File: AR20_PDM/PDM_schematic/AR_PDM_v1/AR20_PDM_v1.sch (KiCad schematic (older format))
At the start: 23 parts, among them J1 S_T_?, J2 1-776163-1, U1 ACM_2020

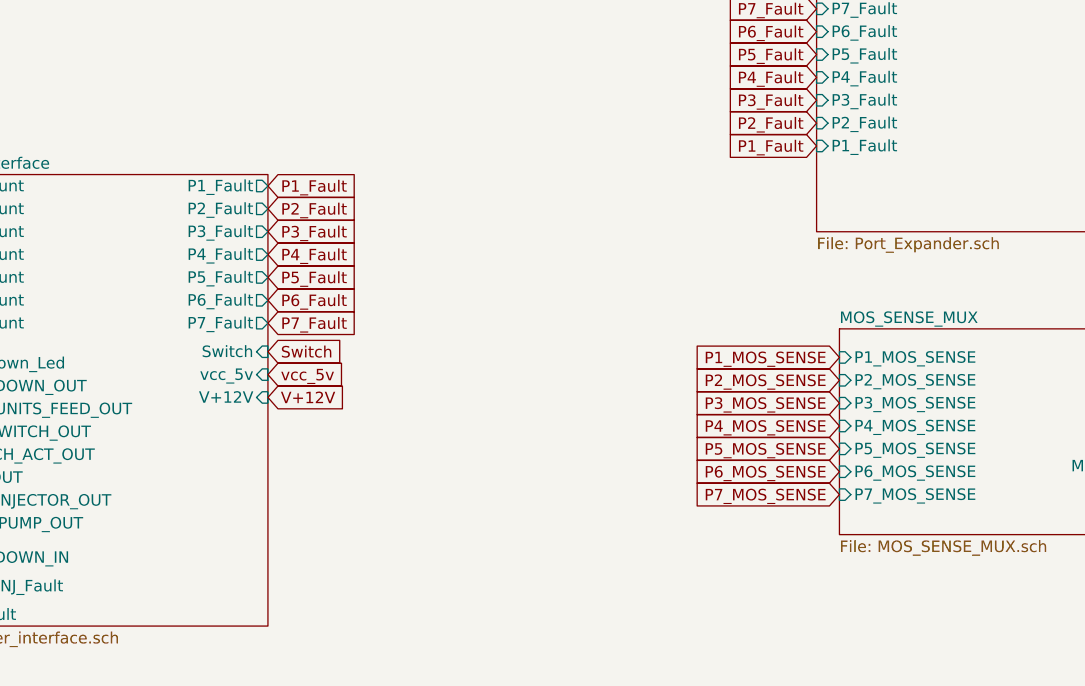
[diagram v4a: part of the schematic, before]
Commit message: Further testing, reveals pdm needs rework
-  As of now, there are major errors in schematics.
- Needs rework. Version charlie postponed.
- Very nice pcb layout thats almost finished. 
   worth noting this layout for the future
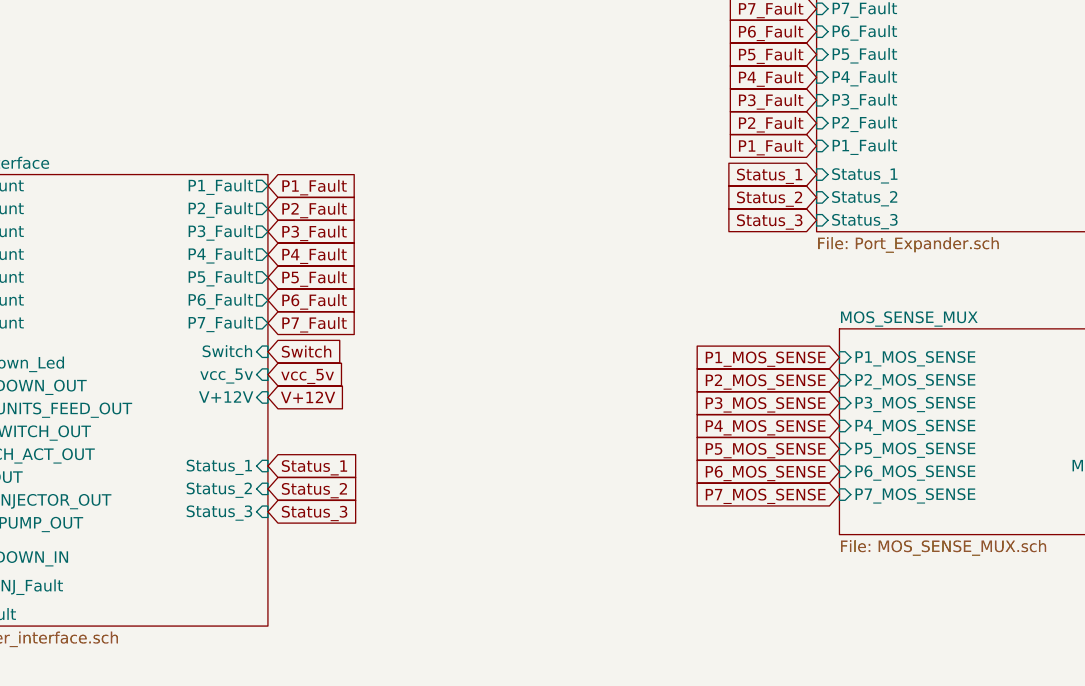
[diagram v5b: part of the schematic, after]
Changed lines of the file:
@@
 F28 "P7_Shunt" I L 4375 4650 50
 F29 "P1_Shunt" I L 4375 4050 50
+F30 "Status_2" I R 5825 5375 50
+F31 "Status_1" I R 5825 5275 50
+F32 "Status_3" I R 5825 5475 50
 $EndSheet
 Text GLabel 10050 3200 2    50   Input ~ 0
@@
 F17 "Mux_select_A2" I R 10050 3400 50
 F18 "Mux_enable" I R 10050 3500 50
+F19 "Status_2" I L 8225 4100 50
+F20 "Status_1" I L 8225 4000 50
+F21 "Status_3" I L 8225 4200 50
 $EndSheet
 NoConn ~ 7900 1275
@@
 Text GLabel 11850 2850 1    50   Input ~ 0
 vcc_5v
+Text GLabel 5825 5275 2    50   Input ~ 0
+Status_1
+Text GLabel 5825 5375 2    50   Input ~ 0
+Status_2
+Text GLabel 5825 5475 2    50   Input ~ 0
+Status_3
+Text GLabel 8225 4000 0    50   Input ~ 0
+Status_1
+Text GLabel 8225 4100 0    50   Input ~ 0
+Status_2
+Text GLabel 8225 4200 0    50   Input ~ 0
+Status_3
 $EndSCHEMATC

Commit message: schematics rework
Fixed INA233 frying due to inductive flyback:
- Paced ina233 high side of the mosftets
- New input protection reseistors, and zener diodes, on each ina233.
Simplified:
- Removed the MUX and mos sense lines, as i realize that most of this functionality can be obtained trough INA233.
- Removed some of the cappacitors , besides the most needed ones.
- removed  back to back zener diode configuration, now a single diode insted.
 to reduce negative voltage in case of loss of VS, to be easy on the INA233 filters.
new stuff:
- Another temp sensor.
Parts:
- removed C4, C5: 470uf, AR_PDM_v1:CAPAE1350X1400N_EEV-FK1V471Q, symbol AR20_PDM_v1-rescue:CP1
- removed C6: 10nf, Capacitor_SMD:C_0603_1608Metric, symbol AR20_PDM_v1-rescue:C-Device
- removed D2, D4: 3.3-5V 5W, Diode_THT:D_5W_P10.16mm_Horizontal, symbol AR20_PDM_v1-rescue:D_Flyback-Zener
- removed R1: 1k, Resistor_SMD:R_0603_1608Metric, symbol AR20_PDM_v1-rescue:R-Device
- removed R2: 4k7, Resistor_SMD:R_0603_1608Metric, symbol AR20_PDM_v1-rescue:R-Device
- added C?: 4.7uF, Capacitor_SMD:C_1206_3216Metric, symbol AR20_PDM_v1-rescue:C-Device
- added R?: 3.9R, Resistor_SMD:R_2512_6332Metric, symbol AR20_PDM_v1-rescue:R-Device
- added R?: NTC, Resistor_SMD:R_0603_1608Metric, symbol AR20_PDM_v1-rescue:R-Device
- added R?: 1k, Resistor_SMD:R_0603_1608Metric, symbol AR20_PDM_v1-rescue:R-Device
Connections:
- net GND: now also D1.2 (A), D3.2 (A), U1.19 (GND), U1.9 (GND), C?.1, R?.1
- net V+12V: now also R?.1
- net vcc_5v: now also R?.1
- net at U1.5 (ADC7): now also R?.2, R?.2
- new net: C?.2, R?.2
- no-connect marks 12 -> 10
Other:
- note added: "Snubber to prevent,\nOscillations on VS line.\nApplication note; \nintroduction to PROFET, page 12"
- note added: "eLoss of power, flyback protection. \nPlace relativly near all of the mosfets.\nApplication note; \nintroduction to PROFET, page 12\nTo keep negative voltage spike low, a single diode in series is used.\nTwo for redundancy\n"
- note removed: "Loss of power, flyback protection. \nPlace relativly near all of the mosfets."
- note removed: "Place relativly close to mcu"
- note removed: "Shared sensing circuit for mosfets."
- moved on the sheet: C1, C2, C3, D1, D3, J1, R106, R107

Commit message: Working on pcb layout
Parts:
- gave numbers to parts that had none: 4
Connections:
- no-connect marks 10 -> 17
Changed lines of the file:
@@
 Text GLabel 7900 950  0    50   Input ~ 0
 vcc_5v
-Wire Wire Line
-	2225 875  2125 875
 $Sheet
 S 1100 625  1025 525
@@
 F7 "P1_MOS_SENSE" O R 2125 875 50
 F8 "P1_MOS_IN" O L 1100 1100 50
-F9 "P1_Shunt" I R 2125 1075 50
 $EndSheet
-Text GLabel 2225 875  2    50   Input ~ 0
-P1_MOS_SENSE
 Wire Wire Line
 	1000 1100 1100 1100
@@
 vcc_5v
 Wire Wire Line
-	2225 1650 2125 1650
-Text GLabel 2225 1650 2    50   Input ~ 0
-P2_MOS_SENSE
-Wire Wire Line
 	1000 1875 1100 1875
 Text GLabel 1000 1875 0    50   Input ~ 0
@@
 Text GLabel 1000 1450 0    50   Input ~ 0
 vcc_5v
-Wire Wire Line
-	2225 2400 2125 2400
 $Sheet
 S 1100 2150 1025 525
@@
 F7 "P3_OUT" O R 2125 2500 50
 F8 "P3_MOS_IN" O L 1100 2625 50
-F9 "P3_Shunt" I R 2125 2600 50
 $EndSheet
-Text GLabel 2225 2400 2    50   Input ~ 0
-P3_MOS_SENSE
 Wire Wire Line
 	1000 2625 1100 2625
@@
 vcc_5v
 Wire Wire Line
-	2225 3150 2125 3150
-Text GLabel 2225 3150 2    50   Input ~ 0
-P4_MOS_SENSE
-Wire Wire Line
 	1000 3375 1100 3375
 Text GLabel 1000 3375 0    50   Input ~ 0
@@
 Text GLabel 1000 2950 0    50   Input ~ 0
 vcc_5v
-Wire Wire Line
-	2225 3900 2125 3900
 $Sheet
 S 1100 3650 1025 525
@@
 F7 "P5_OUT" O R 2125 4000 50
 F8 "P5_MOS_IN" O L 1100 4125 50
-F9 "P5_Shunt" I R 2125 4100 50
 $EndSheet
-Text GLabel 2225 3900 2    50   Input ~ 0
-P5_MOS_SENSE
 Wire Wire Line
 	1000 4125 1100 4125
@@
 Text GLabel 1000 3700 0    50   Input ~ 0
 vcc_5v
-Wire Wire Line
-	2225 4650 2125 4650
 $Sheet
 S 1100 4400 1025 525
@@
 F8 "P6_MOS_IN" O L 1100 4875 50
 F9 "P6_O_D_out" I R 2125 4475 50
-F10 "P6_Shunt" I R 2125 4850 50
 $EndSheet
-Text GLabel 2225 4650 2    50   Input ~ 0
-P6_MOS_SENSE
 Wire Wire Line
 	1000 4875 1100 4875
@@
 Wire Wire Line
 	1125 9100 1125 8850
-Wire Wire Line
-	2225 5400 2125 5400
-Text GLabel 2225 5400 2    50   Input ~ 0
-P7_MOS_SENSE
 Wire Wire Line
 	1000 5625 1100 5625
@@
 F7 "P2_OUT" O R 2125 1750 50
 F8 "P2_MOS_IN" O L 1100 1875 50
-F9 "P2_Shunt" I R 2125 1850 50
 $EndSheet
 $Sheet
@@
 F7 "P4_OUT" O R 2125 3250 50
 F8 "P4_MOS_IN" O L 1100 3375 50
-F9 "P4_Shunt" I R 2125 3350 50
 $EndSheet
 $Sheet
@@
 F7 "P7_OUT" O R 2125 5500 50
 F8 "P7_MOS_IN" O L 1100 5625 50
-F9 "P7_Shunt" I R 2125 5600 50
 $EndSheet
 Wire Wire Line
@@
 Wire Wire Line
 	2225 4750 2125 4750
-Text GLabel 2225 4000 2    50   Input ~ 0
-P5_OUT
-Wire Wire Line
-	2225 4000 2125 4000
 Text GLabel 2225 3250 2    50   Input ~ 0
 P4_OUT
@@
 Text GLabel 8000 750  0    50   Input ~ 0
 SHUTDOWN_IN
-Text GLabel 4375 4650 0    50   Input ~ 0
-P7_Shunt
-Text GLabel 4375 4550 0    50   Input ~ 0
-P6_Shunt
-Text GLabel 4375 4450 0    50   Input ~ 0
-P5_Shunt
-Text GLabel 4375 4350 0    50   Input ~ 0
-P4_Shunt
-Text GLabel 4375 4250 0    50   Input ~ 0
-P3_Shunt
-Text GLabel 4375 4150 0    50   Input ~ 0
-P2_Shunt
-Text GLabel 4375 4050 0    50   Input ~ 0
-P1_Shunt
 Text GLabel 4375 5425 0    50   Input ~ 0
 COIL_INJECTOR_OUT
@@
 Wire Wire Line
 	11425 8475 11425 8675
-Text GLabel 2225 5600 2    50   Input ~ 0
-P7_Shunt
-Text GLabel 2225 4850 2    50   Input ~ 0
-P6_Shunt
-Text GLabel 2225 4100 2    50   Input ~ 0
-P5_Shunt
-Text GLabel 2225 3350 2    50   Input ~ 0
-P4_Shunt
-Text GLabel 2225 2600 2    50   Input ~ 0
-P3_Shunt
-Text GLabel 2225 1850 2    50   Input ~ 0
-P2_Shunt
-Text GLabel 2225 1075 2    50   Input ~ 0
-P1_Shunt
-Wire Wire Line
-	2225 5600 2125 5600
-Wire Wire Line
-	2225 4850 2125 4850
-Wire Wire Line
-	2225 4100 2125 4100
-Wire Wire Line
-	2225 3350 2125 3350
-Wire Wire Line
-	2225 2600 2125 2600
-Wire Wire Line
-	2225 1850 2125 1850
-Wire Wire Line
-	2225 1075 2125 1075
 Text GLabel 13625 975  0    50   Input ~ 0
 P6_EN_ACM
@@
 F21 "Shutdown_Led" I L 4375 4825 50
 F22 "SHUTDOWN_IN" I L 4375 5675 50
-F23 "P2_Shunt" I L 4375 4150 50
-F24 "P3_Shunt" I L 4375 4250 50
-F25 "P4_Shunt" I L 4375 4350 50
-F26 "P5_Shunt" I L 4375 4450 50
-F27 "P6_Shunt" I L 4375 4550 50
-F28 "P7_Shunt" I L 4375 4650 50
-F29 "P1_Shunt" I L 4375 4050 50
-F30 "Status_2" I R 5825 5375 50
-F31 "Status_1" I R 5825 5275 50
-F32 "Status_3" I R 5825 5475 50
+F23 "Status_2" I R 5825 5375 50
+F24 "Status_1" I R 5825 5275 50
+F25 "Status_3" I R 5825 5475 50
+F26 "P2_OUT" I L 4375 4175 50
+F27 "P3_OUT" I L 4375 4275 50
+F28 "P4_OUT" I L 4375 4375 50
+F29 "P5_OUT" I L 4375 4475 50
+F30 "P6_OUT" I L 4375 4575 50
+F31 "P7_OUT" I L 4375 4675 50
+F32 "P1_OUT" I L 4375 4075 50
 $EndSheet
 Text GLabel 15175 2475 2    50   Input ~ 0
@@
 AR Path="/5E0FDCCC/5EE38514" Ref="C?"  Part="1"
 AR Path="/5E10174B/5EE38514" Ref="C?"  Part="1"
-AR Path="/5EE38514" Ref="C?"  Part="1"
-F 0 "C?" H 6165 9246 50  0000 L CNN
+AR Path="/5EE38514" Ref="C4"  Part="1"
+F 0 "C4" H 6165 9246 50  0000 L CNN
 F 1 "4.7uF" H 6165 9155 50  0000 L CNN
 F 2 "Capacitor_SMD:C_1206_3216Metric" H 6088 9050 50  0001 C CNN
@@
 AR Path="/5E0FDCCC/5EE3851A" Ref="#PWR?"  Part="1"
 AR Path="/5E10174B/5EE3851A" Ref="#PWR?"  Part="1"
-AR Path="/5EE3851A" Ref="#PWR?"  Part="1"
-F 0 "#PWR?" H 6050 9150 50  0001 C CNN
+AR Path="/5EE3851A" Ref="#PWR0103"  Part="1"
+F 0 "#PWR0103" H 6050 9150 50  0001 C CNN
 F 1 "GND" H 6055 9227 50  0000 C CNN
 F 2 "" H 6050 9400 50  0001 C CNN
@@
 AR Path="/5E0FDCCC/5EE38522" Ref="R?"  Part="1"
 AR Path="/5E10174B/5EE38522" Ref="R?"  Part="1"
-AR Path="/5EE38522" Ref="R?"  Part="1"
-F 0 "R?" V 5843 8850 50  0000 C CNN
+AR Path="/5EE38522" Ref="R1"  Part="1"
+F 0 "R1" V 5843 8850 50  0000 C CNN
 F 1 "3.9R" V 5934 8850 50  0000 C CNN
 F 2 "Resistor_SMD:R_2512_6332Metric" V 5980 8850 50  0001 C CNN
@@
 AR Path="/5E0FDCCC/5EF487B4" Ref="R?"  Part="1"
 AR Path="/5E10174B/5EF487B4" Ref="R?"  Part="1"
-AR Path="/5EF487B4" Ref="R?"  Part="1"
-F 0 "R?" H 12045 1471 50  0000 L CNN
+AR Path="/5EF487B4" Ref="R2"  Part="1"
+F 0 "R2" H 12045 1471 50  0000 L CNN
 F 1 "NTC" H 12045 1380 50  0000 L CNN
 F 2 "Resistor_SMD:R_0603_1608Metric" V 11905 1425 50  0001 C CNN
@@
 AR Path="/5E0FDCCC/5EF487BB" Ref="#PWR?"  Part="1"
 AR Path="/5E10174B/5EF487BB" Ref="#PWR?"  Part="1"
-AR Path="/5EF487BB" Ref="#PWR?"  Part="1"
-F 0 "#PWR?" H 12425 1475 50  0001 C CNN
+AR Path="/5EF487BB" Ref="#PWR0104"  Part="1"
+F 0 "#PWR0104" H 12425 1475 50  0001 C CNN
 F 1 "GND" H 12430 1552 50  0000 C CNN
 F 2 "" H 12425 1725 50  0001 C CNN
@@
 AR Path="/5E0FDCCC/5EF487C1" Ref="R?"  Part="1"
 AR Path="/5E10174B/5EF487C1" Ref="R?"  Part="1"
-AR Path="/5EF487C1" Ref="R?"  Part="1"
-F 0 "R?" H 12495 1621 50  0000 L CNN
+AR Path="/5EF487C1" Ref="R7"  Part="1"
+F 0 "R7" H 12495 1621 50  0000 L CNN
 F 1 "1k" H 12495 1530 50  0000 L CNN
 F 2 "Resistor_SMD:R_0603_1608Metric" V 12355 1575 50  0001 C CNN
@@
 AR Path="/5DA8920B/5EF84E64" Ref="#PWR?"  Part="1"
 AR Path="/5DE4D361/5EF84E64" Ref="#PWR?"  Part="1"
-AR Path="/5EF84E64" Ref="#PWR?"  Part="1"
-F 0 "#PWR?" H 15175 1025 50  0001 C CNN
+AR Path="/5EF84E64" Ref="#PWR0119"  Part="1"
+F 0 "#PWR0119" H 15175 1025 50  0001 C CNN
 F 1 "GND" V 15175 1075 50  0000 C CNN
 F 2 "" H 15175 1275 50  0001 C CNN
@@
 AR Path="/5DA8920B/5EF85090" Ref="#PWR?"  Part="1"
 AR Path="/5DE4D361/5EF85090" Ref="#PWR?"  Part="1"
-AR Path="/5EF85090" Ref="#PWR?"  Part="1"
-F 0 "#PWR?" H 13625 1775 50  0001 C CNN
+AR Path="/5EF85090" Ref="#PWR0167"  Part="1"
+F 0 "#PWR0167" H 13625 1775 50  0001 C CNN
 F 1 "GND" V 13625 1825 50  0000 C CNN
 F 2 "" H 13625 2025 50  0001 C CNN
@@
 	0    1    1    0
 $EndComp
+Wire Wire Line
+	2225 4000 2125 4000
+Text GLabel 2225 4000 2    50   Input ~ 0
+P5_OUT
+NoConn ~ 2125 875
+NoConn ~ 2125 1650
+NoConn ~ 2125 2400
+NoConn ~ 2125 3150
+NoConn ~ 2125 3900
+NoConn ~ 2125 4650
+NoConn ~ 2125 5400
+Text GLabel 4375 4375 0    50   Input ~ 0
+P4_OUT
+Text GLabel 4375 4275 0    50   Input ~ 0
+P3_OUT
+Text GLabel 4375 4175 0    50   Input ~ 0
+P2_OUT
+Text GLabel 4375 4075 0    50   Input ~ 0
+P1_OUT
+Text GLabel 4375 4475 0    50   Input ~ 0
+P5_OUT
+Text GLabel 4375 4675 0    50   Input ~ 0
+P7_OUT
+Text GLabel 4375 4575 0    50   Input ~ 0
+P6_OUT
 $EndSCHEMATC
